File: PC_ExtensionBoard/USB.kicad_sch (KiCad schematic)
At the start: 81 parts, among them U1 HC-USB3.0-L168-WP, U10 AP22615A_TSOT26, U11 ALC662, U13 AP22615A_TSOT26, U14 ESD204DQAR, U15 AP22615A_TSOT26, U16 ESD204DQAR, U17 AP22615A_TSOT26, U18 ESD204DQAR, U7 HC-USB3.0-L168-WP, U8 ESD204DQAR

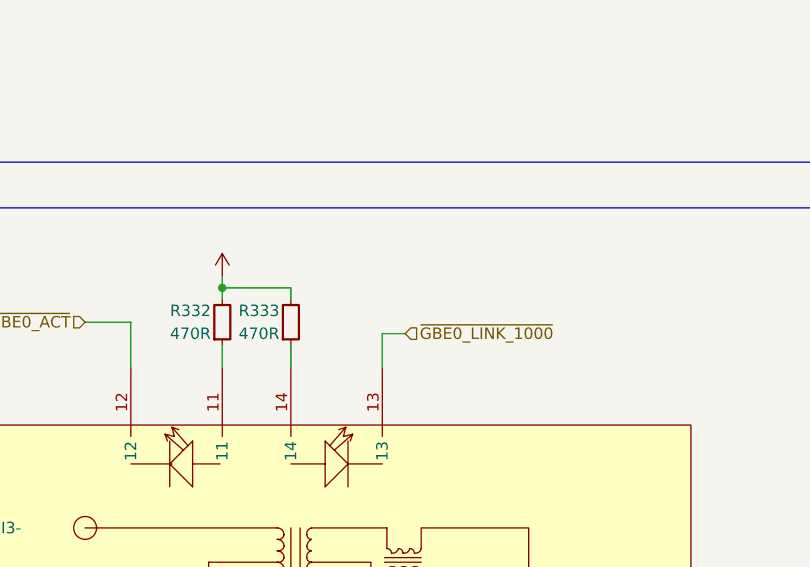
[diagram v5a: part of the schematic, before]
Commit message: update schematic
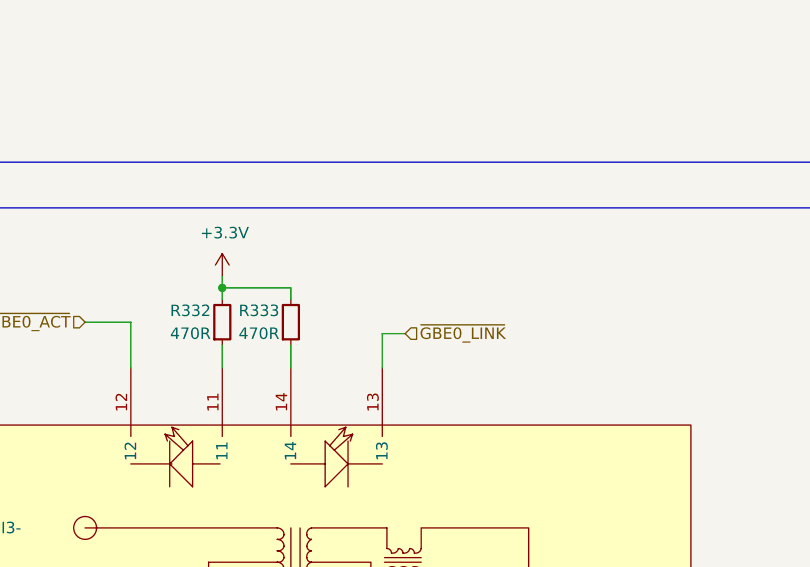
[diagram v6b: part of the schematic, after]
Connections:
- net ~{GBE0_LINK_1000} renamed ~{GBE0_LINK}
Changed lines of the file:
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@@
 		)
 	)
-	(hierarchical_label "~{GBE0_LINK_1000}"
+	(hierarchical_label "~{GBE0_LINK}"
 		(shape input)
 		(at 709.93 424.18 0)
@@
 		(property "Value" "+3.3V"
 			(at 689.864 413.004 0)
-			(hide yes)
 			(show_name no)
 			(do_not_autoplace no)

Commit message: update LCSC Number
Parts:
- added C68: C_1u_0402, PC_Components_1:C_0402_1005Metric, symbol A_PC_ExtensionBoard:C_1u_0402
- added R34: 2.2K/1%, PC_Components_1:R_0402_1005Metric, symbol A_PC_ExtensionBoard:R
- added U22: ESD204DQAR, PC_Components_1:USON-10_2.5x1mm_P0.5mm, symbol A_PC_ExtensionBoard:ESD204DQAR
- RJ1: footprint C54408:RJ45-TH_HR911130A -> PC_Components_1:RJ45-TH_HR911130A
- U1, U7: LCSC (none) -> C7501850
- USB1: LCSC (none) -> C7501881; SUPPLIER PART C7501881 -> (none)
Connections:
- net GND: now also U22.3, U22.8
- net MIC1-VREF0-L: now also R34.1; no longer Audio1.1, U11.21 (MIC1-L)
- net at Audio1.2, U11.35 (FRONT-L): now also U22.2, U22.9
- net at Audio1.3, U11.36 (FRONT-R): now also U22.4, U22.7
- net at Audio1.5, U11.13 (Sense_A): now also U22.5, U22.6
- net BITCLK renamed HDA.BITCLK
- net RST renamed HDA.RST
- net SDIN0 renamed HDA.SDIN0
- net SDOUT renamed HDA.SDOUT
- net SYNC renamed HDA.SYNC
- new net: Audio1.1, C68.1, R34.2, U22.1, U22.10
- new net: C68.2, U11.21 (MIC1-L)
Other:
- moved on the sheet: Audio1, C35, C36, C60, C63, C65, R79, U11B, U11C

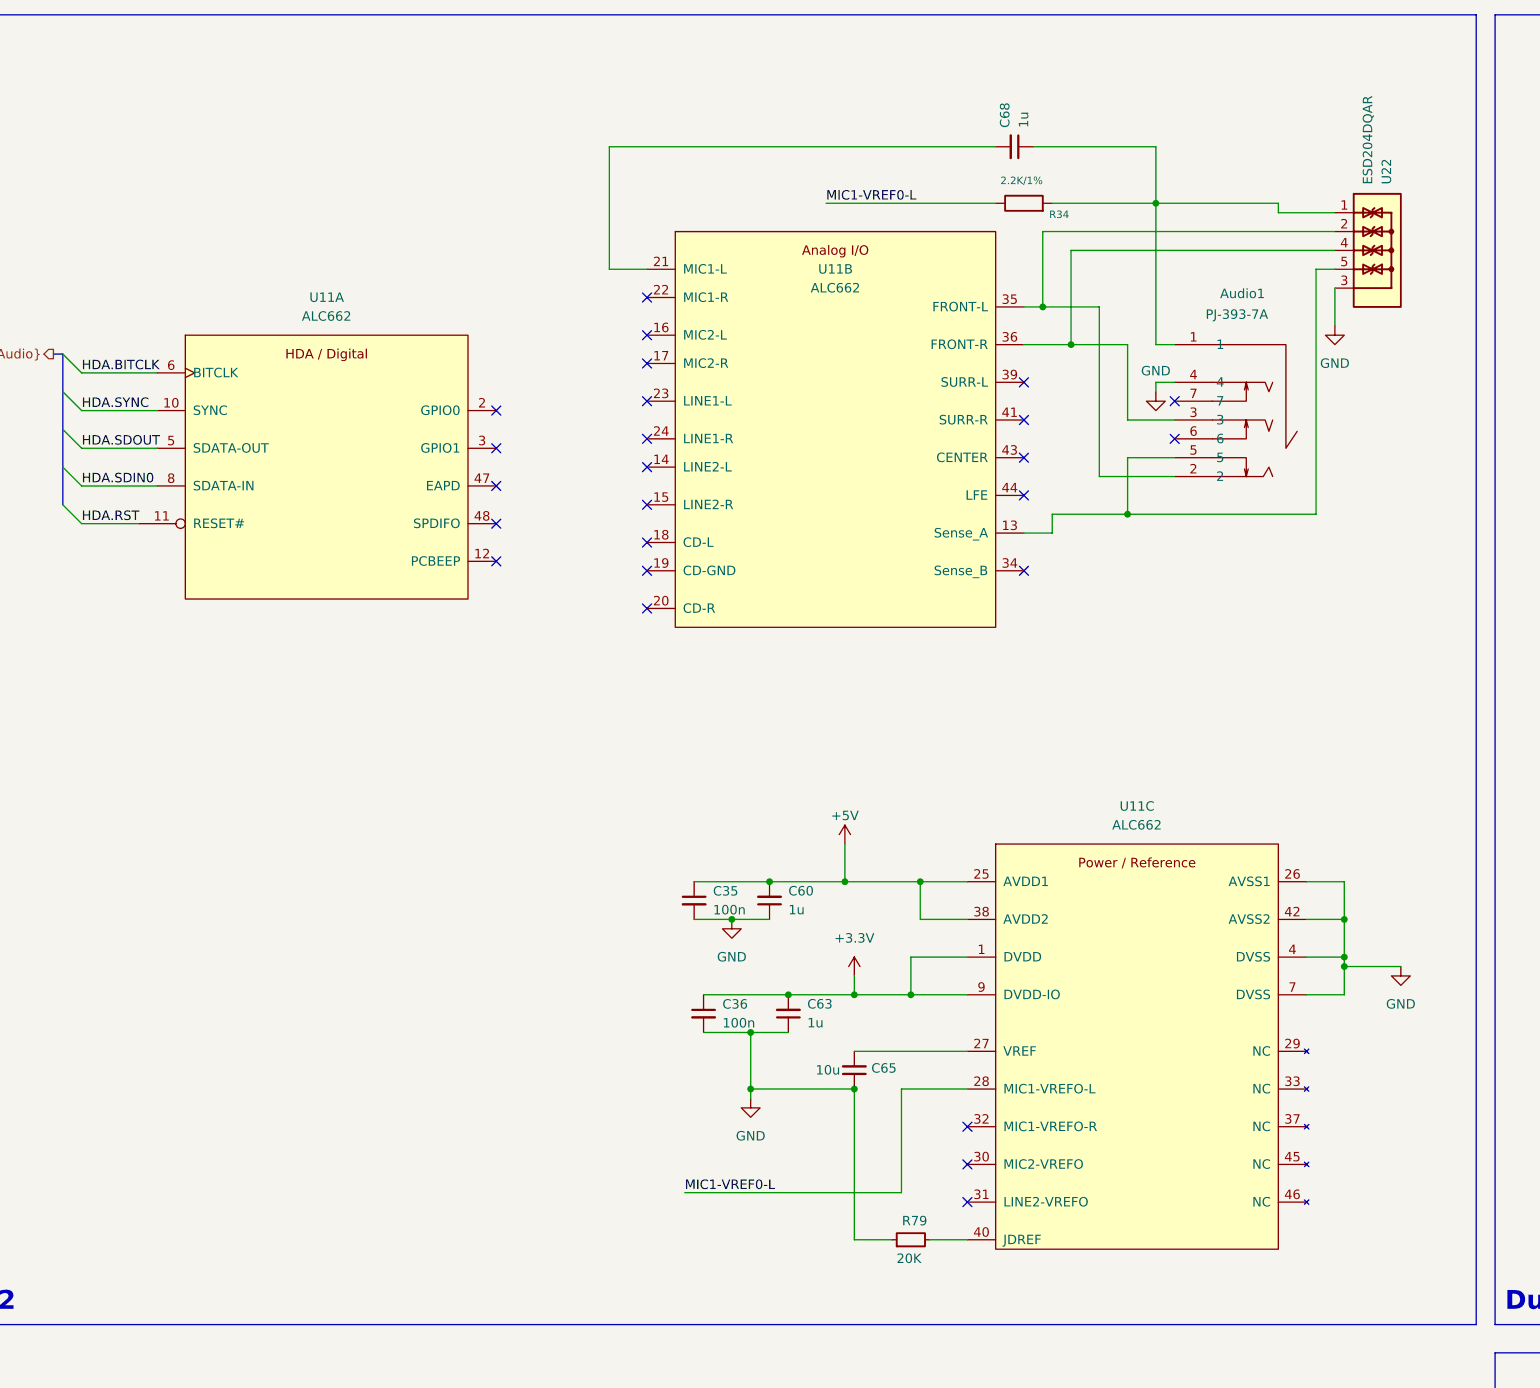
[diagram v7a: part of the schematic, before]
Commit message: update diff pair routing
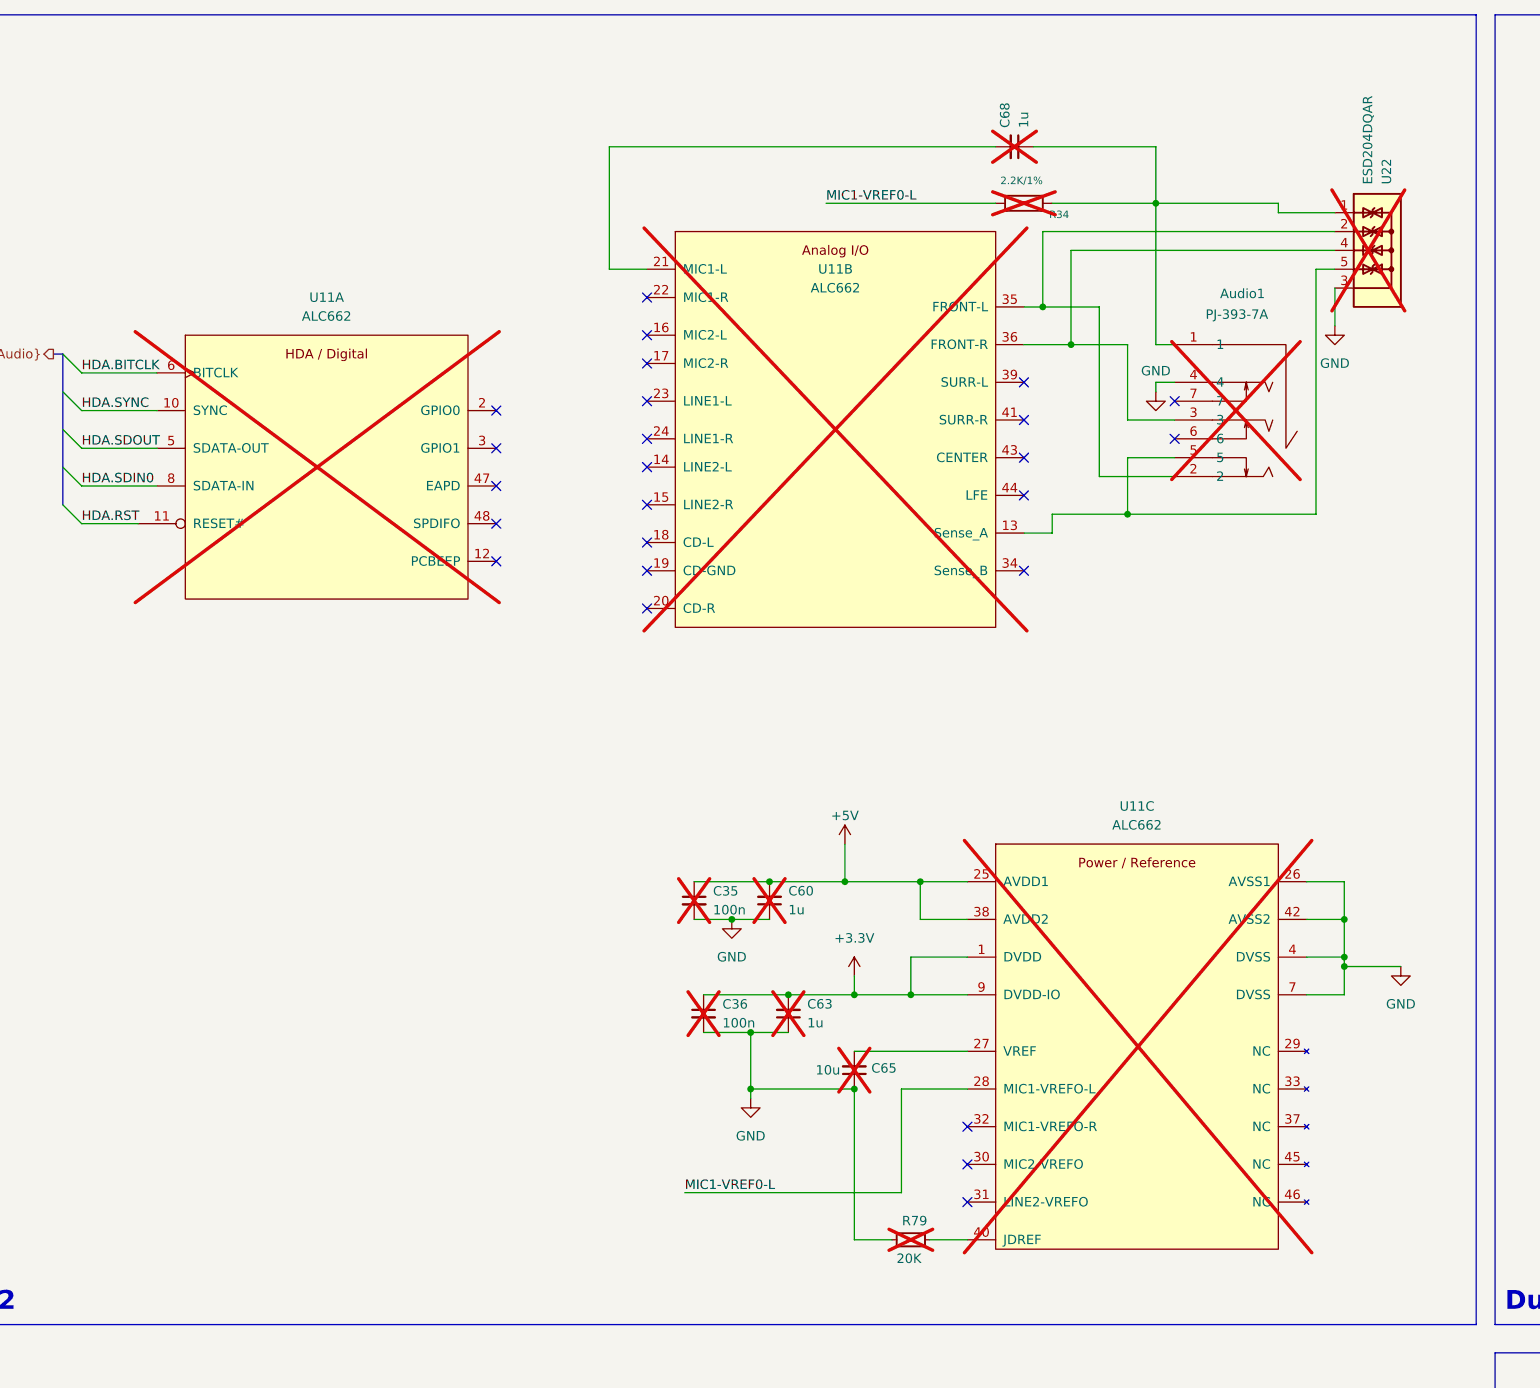
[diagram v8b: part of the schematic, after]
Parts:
- Audio1, C35, C36, C60, C63, C65, C68, R34, R79, U11, U22: now not fitted; now left out of the parts list
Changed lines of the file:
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@@
 		(body_style 1)
 		(exclude_from_sim no)
-		(in_bom yes)
-		(on_board yes)
-		(in_pos_files yes)
-		(dnp no)
+		(in_bom no)
+		(on_board no)
+		(in_pos_files no)
+		(dnp yes)
 		(property "Reference" "Audio1"
 			(at 518.414 50.292 0)
@@
 		(body_style 1)
 		(exclude_from_sim no)
-		(in_bom yes)
-		(on_board yes)
-		(in_pos_files yes)
-		(dnp no)
+		(in_bom no)
+		(on_board no)
+		(in_pos_files no)
+		(dnp yes)
 		(property "Reference" "R34"
 			(at 495.046 39.624 90)
@@
 		(body_style 1)
 		(exclude_from_sim no)
-		(in_bom yes)
-		(on_board yes)
-		(in_pos_files yes)
-		(dnp no)
+		(in_bom no)
+		(on_board no)
+		(in_pos_files no)
+		(dnp yes)
 		(fields_autoplaced yes)
 		(property "Reference" "C36"
@@
 		(body_style 1)
 		(exclude_from_sim no)
-		(in_bom yes)
-		(on_board yes)
-		(in_pos_files yes)
-		(dnp no)
+		(in_bom no)
+		(on_board no)
+		(in_pos_files no)
+		(dnp yes)
 		(property "Reference" "C60"
 			(at 457.2 130.8035 90)
@@
 		(body_style 1)
 		(exclude_from_sim no)
-		(in_bom yes)
-		(on_board yes)
-		(in_pos_files yes)
-		(dnp no)
+		(in_bom no)
+		(on_board no)
+		(in_pos_files no)
+		(dnp yes)
 		(property "Reference" "C65"
 			(at 468.376 154.686 90)
@@
 		(body_style 1)
 		(exclude_from_sim no)
-		(in_bom yes)
-		(on_board yes)
-		(in_pos_files yes)
-		(dnp no)
+		(in_bom no)
+		(on_board no)
+		(in_pos_files no)
+		(dnp yes)
 		(property "Reference" "C68"
 			(at 486.4035 27.94 90)
@@
 		(body_style 1)
 		(exclude_from_sim no)
-		(in_bom yes)
-		(on_board yes)
+		(in_bom no)
+		(on_board no)
 		(in_pos_files yes)
-		(dnp no)
+		(dnp yes)
 		(fields_autoplaced yes)
 		(property "Reference" "U11"
@@
 		(body_style 1)
 		(exclude_from_sim no)
-		(in_bom yes)
-		(on_board yes)
-		(in_pos_files yes)
-		(dnp no)
+		(in_bom no)
+		(on_board no)
+		(in_pos_files no)
+		(dnp yes)
 		(fields_autoplaced yes)
 		(property "Reference" "U22"
@@
 		(body_style 1)
 		(exclude_from_sim no)
-		(in_bom yes)
-		(on_board yes)
-		(in_pos_files yes)
-		(dnp no)
+		(in_bom no)
+		(on_board no)
+		(in_pos_files no)
+		(dnp yes)
 		(fields_autoplaced yes)
 		(property "Reference" "C35"
@@
 		(body_style 1)
 		(exclude_from_sim no)
-		(in_bom yes)
-		(on_board yes)
+		(in_bom no)
+		(on_board no)
 		(in_pos_files yes)
-		(dnp no)
+		(dnp yes)
 		(fields_autoplaced yes)
 		(property "Reference" "U11"
@@
 		(body_style 1)
 		(exclude_from_sim no)
-		(in_bom yes)
-		(on_board yes)
-		(in_pos_files yes)
-		(dnp no)
+		(in_bom no)
+		(on_board no)
+		(in_pos_files no)
+		(dnp yes)
 		(fields_autoplaced yes)
 		(property "Reference" "U11"
@@
 		(body_style 1)
 		(exclude_from_sim no)
-		(in_bom yes)
-		(on_board yes)
-		(in_pos_files yes)
-		(dnp no)
+		(in_bom no)
+		(on_board no)
+		(in_pos_files no)
+		(dnp yes)
 		(property "Reference" "C63"
 			(at 459.74 146.0435 90)
@@
 		(body_style 1)
 		(exclude_from_sim no)
-		(in_bom yes)
-		(on_board yes)
-		(in_pos_files yes)
-		(dnp no)
+		(in_bom no)
+		(on_board no)
+		(in_pos_files no)
+		(dnp yes)
 		(property "Reference" "R79"
 			(at 474.218 175.26 0)
